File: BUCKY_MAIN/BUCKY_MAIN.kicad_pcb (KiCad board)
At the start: 2 copper layers, 190 x 162.2 mm, 0 parts

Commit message: Finished PCBS
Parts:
- added CAN_CONN: CAN_CONN, Connector_JST:JST_PH_S6B-PH-SM4-TB_1x06-1MP_P2.00mm_Horizontal, F.Cu at (203.9, 106.0)
- added COMPASS: MAG_CONN, Connector_JST:JST_SH_BM04B-SRSS-TB_1x04-1MP_P1.00mm_Vertical, F.Cu at (118.7, 73.0)
- added D1: WS2812B, LED_SMD:LED_WS2812B_PLCC4_5.0x5.0mm_P3.2mm, F.Cu at (188.0, 175.6)
- added D2: WS2812B, LED_SMD:LED_WS2812B_PLCC4_5.0x5.0mm_P3.2mm, F.Cu at (147.0, 175.6)
- added D3: WS2812B, LED_SMD:LED_WS2812B_PLCC4_5.0x5.0mm_P3.2mm, F.Cu at (106.0, 175.6)
- added D4: WS2812B, LED_SMD:LED_WS2812B_PLCC4_5.0x5.0mm_P3.2mm, F.Cu at (56.0, 112.0)
- added D5: WS2812B, LED_SMD:LED_WS2812B_PLCC4_5.0x5.0mm_P3.2mm, F.Cu at (78.3, 52.3)
- added D6: WS2812B, LED_SMD:LED_WS2812B_PLCC4_5.0x5.0mm_P3.2mm, F.Cu at (146.7, 21.2)
- added D7: WS2812B, LED_SMD:LED_WS2812B_PLCC4_5.0x5.0mm_P3.2mm, F.Cu at (215.3, 52.9)
- added D8: WS2812B, LED_SMD:LED_WS2812B_PLCC4_5.0x5.0mm_P3.2mm, F.Cu at (238.0, 111.2)
- added J1: PB, BUCKY_MAIN:BUCKY_POWER, F.Cu at (146.7, 138.7)
- added J2: US_L, Connector_PinSocket_2.54mm:PinSocket_1x04_P2.54mm_Vertical_SMD_Pin1Left, F.Cu at (231.2, 111.2)
- added J4: US_R, Connector_PinSocket_2.54mm:PinSocket_1x04_P2.54mm_Vertical_SMD_Pin1Left, F.Cu at (64.0, 111.8)
- added J6: US_F, Connector_PinSocket_2.54mm:PinSocket_1x04_P2.54mm_Vertical_SMD_Pin1Left, F.Cu at (147.0, 168.5)
- added J7: US_B, Connector_PinSocket_2.54mm:PinSocket_1x04_P2.54mm_Vertical_SMD_Pin1Left, F.Cu at (146.8, 30.0)
- added MOTOR 1: IFX9201SG_BO, BUCKY_MAIN:IFX9201SG_BO, F.Cu at (146.7, 106.0)
- added MOTOR 2: IFX9201SG_BO, BUCKY_MAIN:IFX9201SG_BO, F.Cu at (176.5, 106.0)
- added MOTOR 3: IFX9201SG_BO, BUCKY_MAIN:IFX9201SG_BO, F.Cu at (118.2, 106.0)
- added OLED: OLED_CONN, Connector_PinSocket_2.54mm:PinSocket_1x04_P2.54mm_Vertical_SMD_Pin1Left, F.Cu at (90.4, 100.5)
- added R1: 10k, Resistor_SMD:R_0805_2012Metric_Pad1.20x1.40mm_HandSolder, F.Cu at (176.8, 48.7)
- added R2: 120R, Resistor_SMD:R_0805_2012Metric_Pad1.20x1.40mm_HandSolder, F.Cu at (201.0, 94.5)
- added SW1: BUT, BUCKY_MAIN:EVP-BT2J4A000, F.Cu at (169.1, 47.6)
- added U4: ESP32-DEVKITC-32D, BUCKY_MAIN:MODULE_ESP32-DEVKITC-32D, F.Cu at (147.0, 62.5)
- added U5: SN65HVD230, Package_SO:SOIC-8_3.9x4.9mm_P1.27mm, F.Cu at (194.8, 94.3)
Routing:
- net +12V: track 0.00 -> 704.3 mm
- net +5V: track 0.00 -> 617.8 mm, vias 0 -> 2
- net +3.3V: track 0.00 -> 441.6 mm, vias 0 -> 13
- net /F_TRIG: track 0.00 -> 206.6 mm
- net /F_ECHO: track 0.00 -> 206.5 mm
- net /IS: track 0.00 -> 201.3 mm, vias 0 -> 1
- net /LED: track 0.00 -> 199.3 mm, vias 0 -> 2
- net /ST1: track 0.00 -> 182.9 mm, vias 0 -> 2
- net /L_ECHO: track 0.00 -> 117.4 mm, vias 0 -> 1
- net /L_TRIG: track 0.00 -> 114.1 mm, vias 0 -> 1
- net /R_ECHO: track 0.00 -> 103.3 mm, vias 0 -> 1
- net /R_TRIG: track 0.00 -> 96.9 mm, vias 0 -> 1
- net Net-(D3-Pad2): track 0.00 -> 92.3 mm
- net /CAN_RX: track 0.00 -> 83.2 mm, vias 0 -> 1
- net Net-(D6-Pad2): track 0.00 -> 76.8 mm
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- added copper zone on B.Cu, net GND
- added copper zone on F.Cu, net GND
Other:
- outline, holes or cut-outs redrawn
- board text added: "BUCKY MOTHERBOARD DESIGNED BY PIXELJOCH, 01-2023 V-4.0"
- board text added: "JLCJLCJLCJLC"
- board text added: "Mr Postma approves."
- board text added: "TEAM BUCKY"
- board text added: "TRUST ME, I'M AN ENGINEER"
- board text added: "if you can't figure it out, it's a feature."

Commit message: chore: start on schematics
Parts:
- removed CAN_CONN: CAN_CONN, Connector_JST:JST_PH_S6B-PH-SM4-TB_1x06-1MP_P2.00mm_Horizontal
- removed COMPASS: MAG_CONN, Connector_JST:JST_SH_BM04B-SRSS-TB_1x04-1MP_P1.00mm_Vertical
- removed D1, D2, D3, D4, D5, D6, D7, D8: WS2812B, LED_SMD:LED_WS2812B_PLCC4_5.0x5.0mm_P3.2mm
- removed J1: PB, BUCKY_MAIN:BUCKY_POWER
- removed J6: US_F, Connector_PinSocket_2.54mm:PinSocket_1x04_P2.54mm_Vertical_SMD_Pin1Left
- removed J7: US_B, Connector_PinSocket_2.54mm:PinSocket_1x04_P2.54mm_Vertical_SMD_Pin1Left
- removed OLED: OLED_CONN, Connector_PinSocket_2.54mm:PinSocket_1x04_P2.54mm_Vertical_SMD_Pin1Left
- removed SW1: BUT, BUCKY_MAIN:EVP-BT2J4A000
- added R3: 10000R, Resistor_SMD:R_0402_1005Metric, F.Cu at (139.8, 69.7)
- added R4: 10000R, Resistor_SMD:R_0402_1005Metric, F.Cu at (145.3, 69.7)
- added R5: 10000R, Resistor_SMD:R_0402_1005Metric, F.Cu at (142.7, 69.7)
- added R6: 10000R, Resistor_SMD:R_0402_1005Metric, F.Cu at (157.5, 74.7)
- added U6: ~, BUCKY_MAIN:BUCKY_TOF, F.Cu at (146.6, 19.5)
- added U7: ~, BUCKY_MAIN:BUCKY_TOF, F.Cu at (146.6, 176.5)
- added U8: ~, BUCKY_MAIN:BUCKY_TOF, F.Cu at (239.1, 111.8)
- added U9: PCA9548ADB, BUCKY_MAIN:DB24, F.Cu at (150.5, 75.2)
- J2: value US_L -> MAG_CONN; footprint Connector_PinSocket_2.54mm:PinSocket_1x04_P2.54mm_Vertical_SMD_Pin1Left -> Connector_JST:JST_SH_BM04B-SRSS-TB_1x04-1MP_P1.00mm_Vertical
- J4: value US_R -> Conn_01x10; footprint Connector_PinSocket_2.54mm:PinSocket_1x04_P2.54mm_Vertical_SMD_Pin1Left -> BUCKY_MAIN:CONN10_S10B-PH_JST
- R1: value 10k -> 4700R; footprint Resistor_SMD:R_0805_2012Metric_Pad1.20x1.40mm_HandSolder -> Resistor_SMD:R_0402_1005Metric
- R2: value 120R -> 4700R; footprint Resistor_SMD:R_0805_2012Metric_Pad1.20x1.40mm_HandSolder -> Resistor_SMD:R_0402_1005Metric
- U1: renamed from MOTOR 1
- U2: renamed from MOTOR 2
- U3: renamed from MOTOR 3
- U4: value ESP32-DEVKITC-32D -> ~; footprint BUCKY_MAIN:MODULE_ESP32-DEVKITC-32D -> BUCKY_MAIN:BUCKY_POWER
- U5: value SN65HVD230 -> ~; footprint Package_SO:SOIC-8_3.9x4.9mm_P1.27mm -> BUCKY_MAIN:BUCKY_TOF
- moved U5 141.8 mm to (54.1, 111.8), turned to -90 degrees
- moved J4 138.9 mm to (202.8, 105.7), turned to 90 degrees
- moved U4 76.2 mm to (146.6, 138.7), turned to 0 degrees
- moved J2 55.2 mm to (208.1, 61.1)
- moved R2 50.2 mm to (158.0, 68.6)
- moved R1 28.6 mm to (156.2, 68.6), turned to -90 degrees
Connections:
- J2 pad 2: /L_ECHO -> /SCL
- J2 pad 3: /L_TRIG -> /SDA
- J4 pad 1: GND -> /M2_PWM
- J4 pad 2: /R_ECHO -> /M2_DIR
- J4 pad 3: /R_TRIG -> /M1_PWM
- J4 pad 4: +3.3V -> /M1_DIR
- R1 pad 1: +3.3V -> +5V
- R1 pad 2: /PUSH -> /SDA
- R2 pad 1: /CAN_H -> +5V
- R2 pad 2: /CAN_L -> /SCL
- U1 pad 8: +3.3V -> +5V
- U2 pad 8: +3.3V -> +5V
- U3 pad 8: +3.3V -> +5V
- U4 pad 1: +3.3V -> +12V
- U4 pad 2: unconnected-(U4-Pad2) -> +5V
- U4 pad 3: unconnected-(U4-Pad3) -> GND
- U4 pad 5: unconnected-(U4-Pad5) -> GND
- U5 pad 1: /CAN_TX -> /SDA_0
- U5 pad 2: GND -> /SCL_0
- U5 pad 3: +3.3V -> +5V
- U5 pad 4: /CAN_RX -> GND
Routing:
- net +3.3V: track 441.6 -> 0.00 mm, vias 13 -> 0
- net /F_TRIG: track 206.6 -> 0.00 mm
- net /F_ECHO: track 206.5 -> 0.00 mm
- net /IS: track 201.3 -> 0.00 mm, vias 1 -> 0
- net /LED: track 199.3 -> 0.00 mm, vias 2 -> 0
- net /ST1: track 182.9 -> 0.00 mm, vias 2 -> 0
- net /SCL_2: track 0.00 -> 170.1 mm
- net /SDA_2: track 0.00 -> 169.0 mm
- net /L_ECHO: track 117.4 -> 0.00 mm, vias 1 -> 0
- net /L_TRIG: track 114.1 -> 0.00 mm, vias 1 -> 0
- net +5V: track 617.8 -> 504.5 mm, vias 2 -> 4
- net /SCL_3: track 0.00 -> 111.0 mm, vias 0 -> 2
- net /SCL_0: track 0.00 -> 110.5 mm
- net /SDA_3: track 0.00 -> 109.5 mm, vias 0 -> 2
- net /SDA_0: track 0.00 -> 108.5 mm
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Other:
- outline, holes or cut-outs redrawn
- board text added: "- Team Bucky | every year"
- board text added: "BUCKY MAIN DESIGNED BY koen1711, 05-2024 V-1.0"
- board text added: "buck converter not again"
- board text added: "it works, it will be the best robot{dblquote}"
- board text added: "what can go wrong copy pasting?"
- board text added: "{dblquote}IF"
- board text removed: "BUCKY MOTHERBOARD DESIGNED BY PIXELJOCH, 01-2023 V-4.0"

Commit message: chore: finish main board
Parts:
- removed R1, R2: 4700R, Resistor_SMD:R_0402_1005Metric
- removed R3, R4, R5, R6: 10000R, Resistor_SMD:R_0402_1005Metric
- removed U1, U2, U3: IFX9201SG_BO, BUCKY_MAIN:IFX9201SG_BO
- removed U4: ~, BUCKY_MAIN:BUCKY_POWER
- removed U5, U6, U7, U8: ~, BUCKY_MAIN:BUCKY_TOF
- removed U9: PCA9548ADB, BUCKY_MAIN:DB24
- added A2: Arduino Mega, BUCKY_MAIN:ARDUINO_MEGA, B.Cu at (120.9, 92.3)
- added C1: 10uF, Capacitor_SMD:C_0603_1608Metric, F.Cu at (122.8, 26.6)
- added C10: 10uF, Capacitor_SMD:C_0603_1608Metric, F.Cu at (48.3, 102.3)
- added C11: 10uF, Capacitor_SMD:C_0603_1608Metric, F.Cu at (61.7, 60.1)
- added C12: 10uF, Capacitor_SMD:C_0603_1608Metric, F.Cu at (88.8, 37.0)
- added C2: 10uF, Capacitor_SMD:C_0603_1608Metric, F.Cu at (158.9, 39.1)
- added C3: 10uF, Capacitor_SMD:C_0603_1608Metric, F.Cu at (182.7, 64.7)
- added C4: 10uF, Capacitor_SMD:C_0603_1608Metric, F.Cu at (188.8, 99.9)
- added C5: 10uF, Capacitor_SMD:C_0603_1608Metric, F.Cu at (180.4, 135.5)
- added C6: 10uF, Capacitor_SMD:C_0603_1608Metric, F.Cu at (160.7, 157.2)
- added C7: 10uF, Capacitor_SMD:C_0603_1608Metric, F.Cu at (125.0, 166.9)
- added C8: 10uF, Capacitor_SMD:C_0603_1608Metric, F.Cu at (90.7, 159.2)
- added C9: 10uF, Capacitor_SMD:C_0603_1608Metric, F.Cu at (62.4, 135.4)
- added D1: D, Diode_SMD:D_0603_1608Metric, F.Cu at (119.9, 30.0)
- added D10: D, Diode_SMD:D_0603_1608Metric, F.Cu at (50.1, 98.7)
- added D11: D, Diode_SMD:D_0603_1608Metric, F.Cu at (60.3, 63.5)
- added D12: D, Diode_SMD:D_0603_1608Metric, F.Cu at (87.4, 41.7)
- added D13: D, Diode_SMD:D_0603_1608Metric, F.Cu at (92.7, 125.5)
- added D14: D, Diode_SMD:D_0603_1608Metric, F.Cu at (94.0, 128.3)
- added D2: D, Diode_SMD:D_0603_1608Metric, F.Cu at (153.9, 38.9)
- added D3: D, Diode_SMD:D_0603_1608Metric, F.Cu at (179.6, 62.8)
- added D4: D, Diode_SMD:D_0603_1608Metric, F.Cu at (187.2, 97.3)
- added D5: D, Diode_SMD:D_0603_1608Metric, F.Cu at (179.4, 131.3)
- added D6: D, Diode_SMD:D_0603_1608Metric, F.Cu at (155.8, 157.2)
- added D7: D, Diode_SMD:D_0603_1608Metric, F.Cu at (121.2, 166.1)
- added D8: D, Diode_SMD:D_0603_1608Metric, F.Cu at (87.7, 155.6)
- added D9: D, Diode_SMD:D_0603_1608Metric, F.Cu at (63.7, 131.7)
- added IC1: TSSP96038TR, BUCKY_MAIN:TSSP96038, F.Cu at (120.6, 23.2)
- added IC10 (x2): TSSP96038TR, BUCKY_MAIN:TSSP96038, F.Cu at (46.0, 98.0)
- added IC11: TSSP96038TR, BUCKY_MAIN:TSSP96038, F.Cu at (56.0, 60.7)
- added IC12: TSSP96038TR, BUCKY_MAIN:TSSP96038, F.Cu at (83.3, 33.2)
- added IC2: TSSP96038TR, BUCKY_MAIN:TSSP96038, F.Cu at (158.0, 33.3)
- added IC3: TSSP96038TR, BUCKY_MAIN:TSSP96038, F.Cu at (185.4, 60.7)
- added IC4: TSSP96038TR, BUCKY_MAIN:TSSP96038, F.Cu at (195.5, 98.0)
- added IC5: TSSP96038TR, BUCKY_MAIN:TSSP96038, F.Cu at (185.4, 135.4)
- added IC6: TSSP96038TR, BUCKY_MAIN:TSSP96038, F.Cu at (158.0, 162.7)
- added IC7: TSSP96038TR, BUCKY_MAIN:TSSP96038, F.Cu at (120.6, 172.7)
- added IC8: TSSP96038TR, BUCKY_MAIN:TSSP96038, F.Cu at (83.3, 162.7)
- added IC9: TSSP96038TR, BUCKY_MAIN:TSSP96038, F.Cu at (55.9, 135.4)
- added J1: Conn_01x10, BUCKY_MAIN:CONN10_S10B-PH_JST, F.Cu at (105.2, 133.1)
- added J3: Conn_01x02, BUCKY_MAIN:CONN_S2B-PH-K-S_JST, F.Cu at (88.7, 131.2)
- J2: value MAG_CONN -> Conn_01x16; footprint Connector_JST:JST_SH_BM04B-SRSS-TB_1x04-1MP_P1.00mm_Vertical -> BUCKY_MAIN:CONN_B16B-PH-SM4-TB_JST
- J4: value Conn_01x10 -> Conn_01x06; footprint BUCKY_MAIN:CONN10_S10B-PH_JST -> Connector_PinHeader_2.54mm:PinHeader_1x06_P2.54mm_Horizontal
- moved J2 86.1 mm to (123.0, 48.2)
- moved J4 57.4 mm to (151.4, 131.4), turned to -90 degrees
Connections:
- J2 pad 1: GND -> /R_A
- J2 pad 2: /SCL -> /R_S0
- J2 pad 3: /SDA -> /R_S1
- J2 pad 4: +3.3V -> /R_S2
- J4 pad 1: /M2_PWM -> /STATE
- J4 pad 2: /M2_DIR -> /TXD
- J4 pad 3: /M1_PWM -> /RXD
- J4 pad 4: /M1_DIR -> GND
- J4 pad 5: /M3_PWM -> +5V
- J4 pad 6: /M3_DIR -> /EN
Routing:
- net +12V: track 692.1 -> 0.00 mm
- net +5V: track 504.5 -> 295.4 mm, vias 4 -> 0
- net /SCL_2: track 170.1 -> 0.00 mm
- net /SDA_2: track 169.0 -> 0.00 mm
- net /IR_11: track 0.00 -> 125.4 mm, vias 0 -> 1
- net /IR_12: track 0.00 -> 114.7 mm, vias 0 -> 1
- net /SCL_3: track 111.0 -> 0.00 mm, vias 2 -> 0
- net /SCL_0: track 110.5 -> 0.00 mm
- net /SDA_3: track 109.5 -> 0.00 mm, vias 2 -> 0
- net /SDA_0: track 108.5 -> 0.00 mm
- net /IR_1: track 0.00 -> 88.1 mm, vias 0 -> 1
- net /M3_PWM: track 117.2 -> 32.2 mm, vias 0 -> 1
- net /D_S2: track 0.00 -> 84.5 mm
- net /F_S0: track 0.00 -> 84.2 mm
- net /R_S1: track 0.00 -> 83.3 mm
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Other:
- board size 190 x 162.2 mm -> 156.4 x 156.4 mm
- board text added: "BUCKY MAIN BOARD DESIGNED BY koen1711 7-2024 V-1.0"
- board text added: "EN"
- board text added: "HC05"
- board text added: "MAIN -> DRIVE"
- board text added: "MAIN -> LIGHT"
- board text added: "STATE"
- board text added: "X +5VGND RXD TXD X"
- board text added: "debugability they called it, fuckupability is better"
- board text added: "they said i couldn't do it, i couldn't"
- board text removed: "- Team Bucky | every year"
- board text removed: "BUCKY MAIN DESIGNED BY koen1711, 05-2024 V-1.0"
- board text removed: "JLCJLCJLCJLC"
- board text removed: "Mr Postma approves."
- board text removed: "TRUST ME, I'M AN ENGINEER"
- board text removed: "buck converter not again"
- board text removed: "if you can't figure it out, it's a feature."
- board text removed: "it works, it will be the best robot{dblquote}"
- board text removed: "what can go wrong copy pasting?"
- board text removed: "{dblquote}IF"

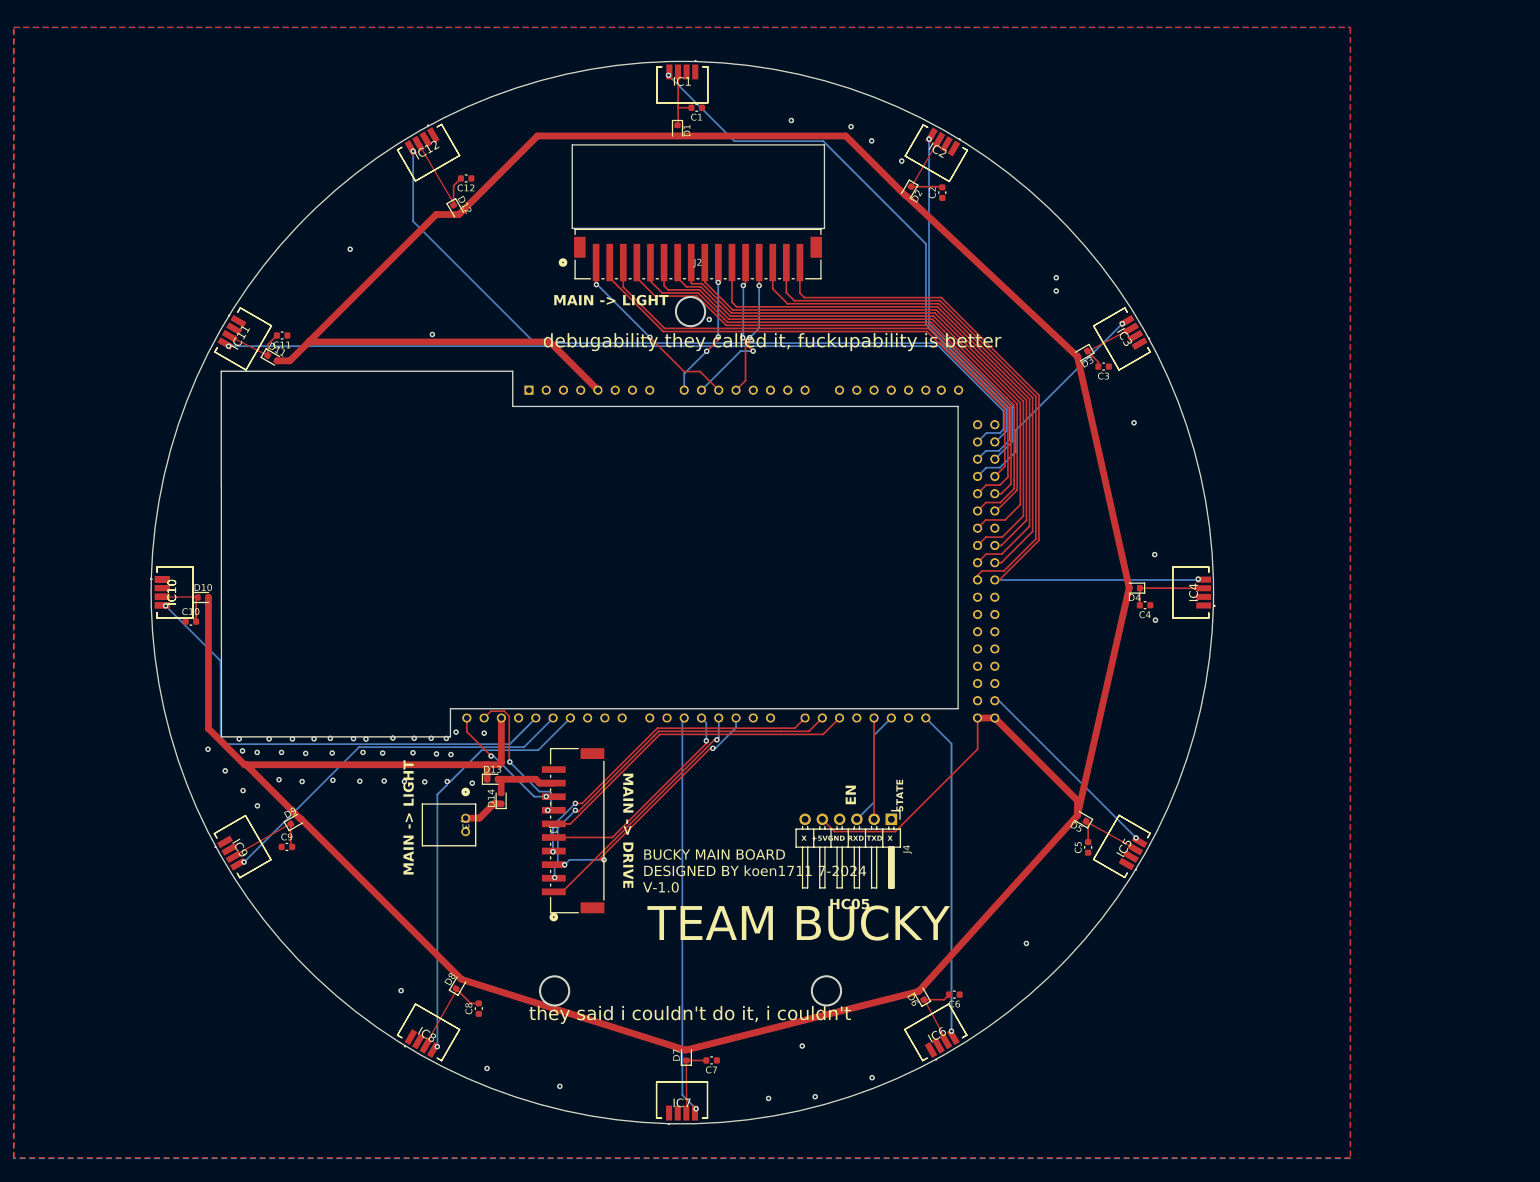
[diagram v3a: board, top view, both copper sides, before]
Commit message: chore: start on ldr instead of Q_Photo_N, interrupt instead of analog multiplexer. And a signal for front,back,left,right
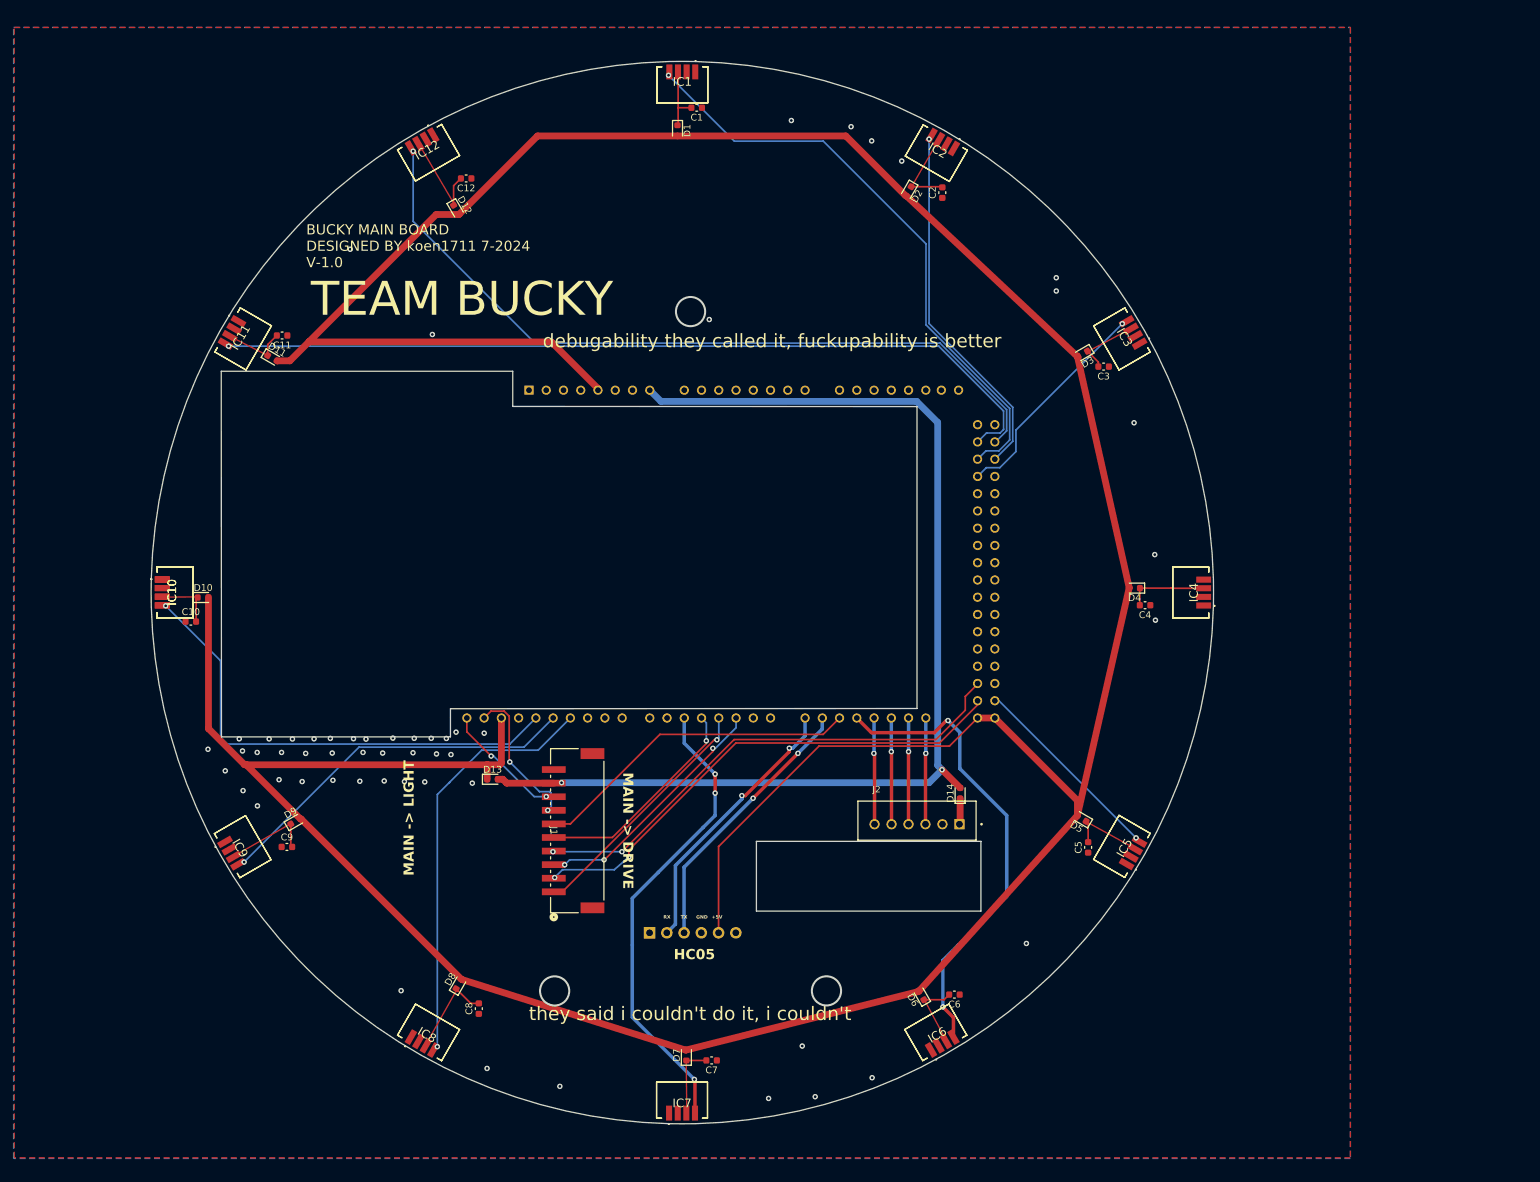
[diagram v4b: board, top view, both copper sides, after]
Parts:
- removed J3: Conn_01x02, BUCKY_MAIN:CONN_S2B-PH-K-S_JST
- J2: value Conn_01x16 -> Conn_01x06; footprint BUCKY_MAIN:CONN_B16B-PH-SM4-TB_JST -> BUCKY_MAIN:LIGHT_CONN
- J4: moved to B.Cu
- moved J2 89.4 mm to (155.2, 131.6)
- moved D14 67.6 mm to (161.5, 127.5)
- moved J4 39.3 mm to (115.8, 148.1)
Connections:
- A2 pad 14: /M1_DIR -> /TXD
- A2 pad 15: /M2_DIR -> /RXD
- A2 pad 17: unconnected-(A2-Pad17) -> /IR_6
- A2 pad 18: /TXD -> /SIG_RIGHT
- A2 pad 19: /RXD -> /SIG_LEFT
- A2 pad 20: unconnected-(A2-Pad20) -> /SIG_BACK
- A2 pad 21: /IR_6 -> /SIG_FRONT
- A2 pad 22: unconnected-(A2-Pad22) -> /M2_DIR
- A2 pad 24: unconnected-(A2-Pad24) -> /M1_DIR
- A2 pad 36: /L_S1 -> unconnected-(A2-Pad36)
- A2 pad 37: /L_S0 -> unconnected-(A2-Pad37)
- A2 pad 38: /F_S0 -> unconnected-(A2-Pad38)
- A2 pad 39: /L_S2 -> unconnected-(A2-Pad39)
- A2 pad 40: /D_S2 -> unconnected-(A2-Pad40)
- A2 pad 41: /D_S1 -> unconnected-(A2-Pad41)
- A2 pad 42: /D_S0 -> unconnected-(A2-Pad42)
- A2 pad 44: /F_S2 -> unconnected-(A2-Pad44)
- A2 pad 45: /F_S1 -> unconnected-(A2-Pad45)
- A2 pad 46: /R_S1 -> unconnected-(A2-Pad46)
- A2 pad 47: /R_S2 -> unconnected-(A2-Pad47)
- A2 pad 49: /R_S0 -> unconnected-(A2-Pad49)
- A2 pad VIN: +5V -> /VIN
- J2 pad 1: /R_A -> Net-(D14-K)
- J2 pad 2: /R_S0 -> GND
- J2 pad 3: /R_S1 -> /SIG_FRONT
- J2 pad 4: /R_S2 -> /SIG_BACK
- J2 pad 5: /F_S2 -> /SIG_LEFT
- J2 pad 6: /F_S1 -> /SIG_RIGHT
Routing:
- net /VIN: track 10.6 -> 165.1 mm, vias 0 -> 2
- net /D_S2: track 84.5 -> 0.00 mm
- net /F_S0: track 84.2 -> 0.00 mm
- net /R_S1: track 83.3 -> 0.00 mm
- net /D_S0: track 83.0 -> 0.00 mm
- net /F_S2: track 82.9 -> 0.00 mm
- net /D_S1: track 81.3 -> 0.00 mm
- net /L_S1: track 80.0 -> 0.00 mm
- net /F_S1: track 79.8 -> 0.00 mm
- net /R_S2: track 79.6 -> 0.00 mm
- net /R_S0: track 78.9 -> 0.00 mm
- net /L_S0: track 76.2 -> 0.00 mm
- net /L_S2: track 75.9 -> 0.00 mm
- net /IR_4: track 30.0 -> 0.00 mm, vias 1 -> 0
- net /R_A: track 28.0 -> 0.00 mm, vias 2 -> 0
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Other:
- outline, holes or cut-outs redrawn
- board text added: "+5V"
- board text added: "GND"
- board text added: "RX"
- board text added: "TX"
- board text removed: "EN"
- board text removed: "STATE"
- board text removed: "X +5VGND RXD TXD X"
